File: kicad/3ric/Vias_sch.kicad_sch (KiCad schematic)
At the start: 7 parts, among them J3 PS/2 keyboard

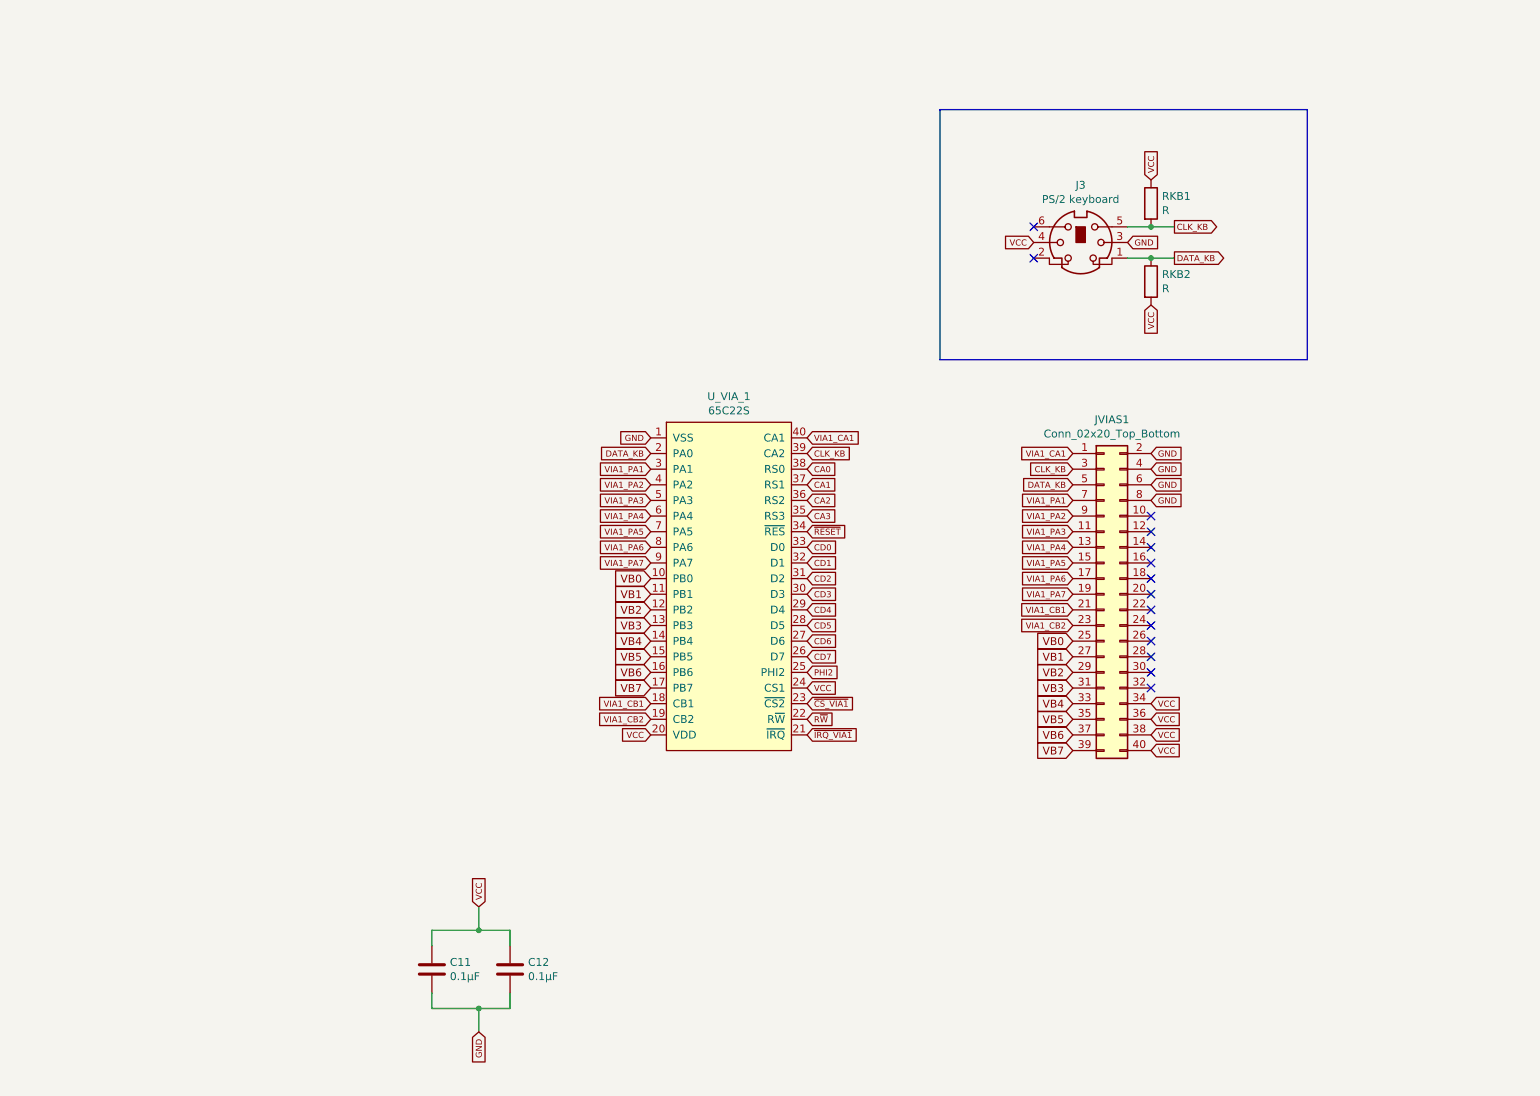
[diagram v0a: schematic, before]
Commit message: schematic updates - bring the schematics up to match breadboard changes current state has high res Apple II color emulation working
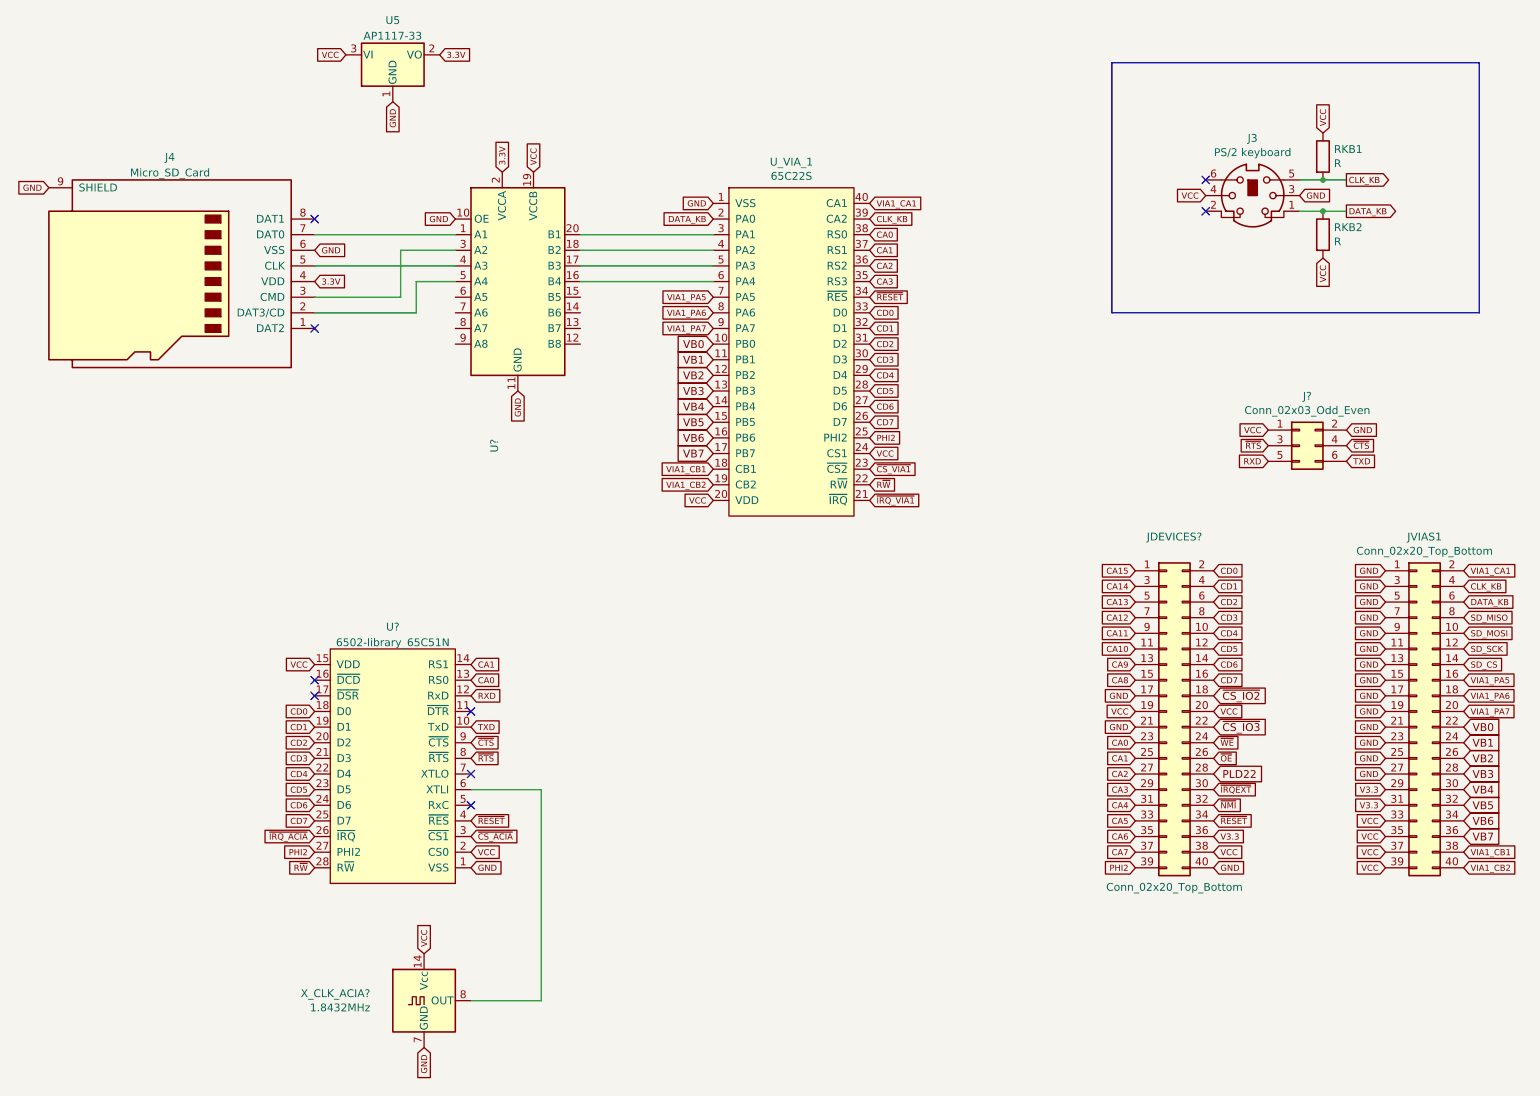
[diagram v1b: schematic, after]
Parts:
- removed C11, C12: 0.1µF, Capacitor_THT:C_Axial_L3.8mm_D2.6mm_P7.50mm_Horizontal, symbol Device:C
- added J4: Micro_SD_Card, badger6502pico:microSD_Amazon2, symbol Connector:Micro_SD_Card
- added J?: Conn_02x03_Odd_Even, Connector_PinHeader_2.54mm:PinHeader_2x03_P2.54mm_Vertical, symbol Connector_Generic:Conn_02x03_Odd_Even
- added JDEVICES?: Conn_02x20_Top_Bottom, Connector_IDC:IDC-Header_2x20_P2.54mm_Vertical, symbol Connector_Generic:Conn_02x20_Odd_Even
- added U5: AP1117-33, Package_TO_SOT_SMD:SOT-223-3_TabPin2, symbol Regulator_Linear:AP1117-33
- added U?: (no value), symbol Logic_LevelTranslator:TXS0108EPW
- added U?: 6502-library_65C51N, Package_DIP:DIP-28_W15.24mm_Socket, symbol EB6502-custom:6502-library_65C51N
- added X_CLK_ACIA?: 1.8432MHz, Oscillator:Oscillator_DIP-14, symbol Oscillator:ACO-xxxMHz
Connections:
- net CA0: now also JDEVICES?.23 (Pin_23), U?.13 (RS0)
- net CA1: now also JDEVICES?.25 (Pin_25), U?.14 (RS1)
- net CA2: now also JDEVICES?.27 (Pin_27)
- net CA3: now also JDEVICES?.29 (Pin_29)
- net CD0: now also JDEVICES?.2 (Pin_2), U?.18 (D0)
- net CD1: now also JDEVICES?.4 (Pin_4), U?.19 (D1)
- net CD2: now also JDEVICES?.6 (Pin_6), U?.20 (D2)
- net CD3: now also JDEVICES?.8 (Pin_8), U?.21 (D3)
- net CD4: now also JDEVICES?.10 (Pin_10), U?.22 (D4)
- net CD5: now also JDEVICES?.12 (Pin_12), U?.23 (D5)
- net CD6: now also JDEVICES?.14 (Pin_14), U?.24 (D6)
- net CD7: now also JDEVICES?.16 (Pin_16), U?.25 (D7)
- net CLK_KB: now also JVIAS1.4 (Pin_4); no longer JVIAS1.3 (Pin_3)
- net DATA_KB: now also JVIAS1.6 (Pin_6); no longer JVIAS1.5 (Pin_5)
- net GND: now also JVIAS1.1 (Pin_1), JVIAS1.11 (Pin_11), JVIAS1.13 (Pin_13), JVIAS1.15 (Pin_15), JVIAS1.17 (Pin_17), JVIAS1.19 (Pin_19), JVIAS1.21 (Pin_21), JVIAS1.23 (Pin_23), JVIAS1.25 (Pin_25), JVIAS1.27 (Pin_27), JVIAS1.3 (Pin_3), JVIAS1.5 (Pin_5), JVIAS1.7 (Pin_7), JVIAS1.9 (Pin_9), J4.6 (VSS), J4.9 (SHIELD), J?.2 (Pin_2), JDEVICES?.17 (Pin_17), JDEVICES?.21 (Pin_21), JDEVICES?.40 (Pin_40), U5.1 (GND), U?.1 (VSS), U?.10 (OE), U?.11 (GND), X_CLK_ACIA?.7 (GND); no longer JVIAS1.2 (Pin_2), JVIAS1.4 (Pin_4), JVIAS1.6 (Pin_6), JVIAS1.8 (Pin_8)
- net PHI2: now also JDEVICES?.39 (Pin_39), U?.27 (PHI2)
- net R~{W}: now also U?.28 (R~{W})
- net VB0: now also JVIAS1.22 (Pin_22); no longer JVIAS1.25 (Pin_25)
- net VB1: now also JVIAS1.24 (Pin_24); no longer JVIAS1.27 (Pin_27)
- net VB2: now also JVIAS1.26 (Pin_26); no longer JVIAS1.29 (Pin_29)
- net VB3: now also JVIAS1.28 (Pin_28); no longer JVIAS1.31 (Pin_31)
- net VB4: now also JVIAS1.30 (Pin_30); no longer JVIAS1.33 (Pin_33)
- net VB5: now also JVIAS1.32 (Pin_32); no longer JVIAS1.35 (Pin_35)
- net VB6: now also JVIAS1.34 (Pin_34); no longer JVIAS1.37 (Pin_37)
- net VB7: now also JVIAS1.36 (Pin_36); no longer JVIAS1.39 (Pin_39)
- net VCC: now also JVIAS1.33 (Pin_33), JVIAS1.35 (Pin_35), JVIAS1.37 (Pin_37), JVIAS1.39 (Pin_39), J?.1 (Pin_1), JDEVICES?.19 (Pin_19), JDEVICES?.20 (Pin_20), JDEVICES?.38 (Pin_38), U5.3 (VI), U?.15 (VDD), U?.19 (VCCB), U?.2 (CS0), X_CLK_ACIA?.14 (Vcc); no longer JVIAS1.34 (Pin_34), JVIAS1.36 (Pin_36), JVIAS1.38 (Pin_38), JVIAS1.40 (Pin_40)
- net VIA1_CA1: now also JVIAS1.2 (Pin_2); no longer JVIAS1.1 (Pin_1)
- net VIA1_CB1: now also JVIAS1.38 (Pin_38); no longer JVIAS1.21 (Pin_21)
- net VIA1_CB2: now also JVIAS1.40 (Pin_40); no longer JVIAS1.23 (Pin_23)
- net VIA1_PA5: now also JVIAS1.16 (Pin_16); no longer JVIAS1.15 (Pin_15)
- net VIA1_PA6: now also JVIAS1.18 (Pin_18); no longer JVIAS1.17 (Pin_17)
- net VIA1_PA7: now also JVIAS1.20 (Pin_20); no longer JVIAS1.19 (Pin_19)
- net ~{RESET}: now also JDEVICES?.34 (Pin_34), U?.4 (~{RES})
- net SD_MOSI: now reaches JVIAS1.10 (Pin_10)
- net SD_SCK: now reaches JVIAS1.12 (Pin_12)
- net SD_CS: now reaches JVIAS1.14 (Pin_14)
- net VIA1_PA1: no longer names the net of U_VIA_1.3 (PA1)
- net VIA1_PA1: now also U?.20 (B1); no longer JVIAS1.7 (Pin_7)
- net VIA1_PA2: no longer names the net of U_VIA_1.4 (PA2)
- net VIA1_PA2: now also U?.18 (B2); no longer JVIAS1.9 (Pin_9)
- net VIA1_PA3: no longer names the net of U_VIA_1.5 (PA3)
- net VIA1_PA3: now also U?.17 (B3); no longer JVIAS1.11 (Pin_11)
- net VIA1_PA4: no longer names the net of U_VIA_1.6 (PA4)
- net VIA1_PA4: now also U?.16 (B4); no longer JVIAS1.13 (Pin_13)
- new net: J4.2 (DAT3/CD), U?.5 (A4)
- new net: J4.3 (CMD), U?.3 (A2)
- new net: J4.5 (CLK), U?.4 (A3)
- new net: J4.7 (DAT0), U?.1 (A1)
- new net: U?.6 (XTLI), X_CLK_ACIA?.8 (OUT)
- new net 3.3V: J4.4 (VDD), U5.2 (VO), U?.2 (VCCA)
- new net CA10: JDEVICES?.11 (Pin_11)
- new net CA11: JDEVICES?.9 (Pin_9)
- new net CA12: JDEVICES?.7 (Pin_7)
- new net CA13: JDEVICES?.5 (Pin_5)
- new net CA14: JDEVICES?.3 (Pin_3)
- new net CA15: JDEVICES?.1 (Pin_1)
- new net CA4: JDEVICES?.31 (Pin_31)
- new net CA5: JDEVICES?.33 (Pin_33)
- new net CA6: JDEVICES?.35 (Pin_35)
- new net CA7: JDEVICES?.37 (Pin_37)
- new net CA8: JDEVICES?.15 (Pin_15)
- new net CA9: JDEVICES?.13 (Pin_13)
- new net PLD22: JDEVICES?.28 (Pin_28)
- new net RXD: J?.5 (Pin_5), U?.12 (RxD)
- new net SD_MISO: JVIAS1.8 (Pin_8)
- new net TXD: J?.6 (Pin_6), U?.10 (TxD)
- new net V3.3: JDEVICES?.36 (Pin_36), JVIAS1.29 (Pin_29), JVIAS1.31 (Pin_31)
- new net ~{CS_ACIA}: U?.3 (~{CS1})
- new net ~{CS_IO2}: JDEVICES?.18 (Pin_18)
- new net ~{CS_IO3}: JDEVICES?.22 (Pin_22)
- new net ~{CTS}: J?.4 (Pin_4), U?.9 (~{CTS})
- new net ~{IRQEXT}: JDEVICES?.30 (Pin_30)
- new net ~{IRQ_ACIA}: U?.26 (~{IRQ})
- new net ~{NMI}: JDEVICES?.32 (Pin_32)
- new net ~{OE}: JDEVICES?.26 (Pin_26)
- new net ~{RTS}: J?.3 (Pin_3), U?.8 (~{RTS})
- new net ~{WE}: JDEVICES?.24 (Pin_24)
- no-connect marks 14 -> 9
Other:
- moved on the sheet: J3, JVIAS1, RKB1, RKB2, U_VIA_1
